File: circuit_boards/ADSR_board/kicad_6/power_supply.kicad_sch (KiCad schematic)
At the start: 21 parts, among them J5 power_entry, U101 TL072, U201 TL072, U301 TL072, U401 TL072

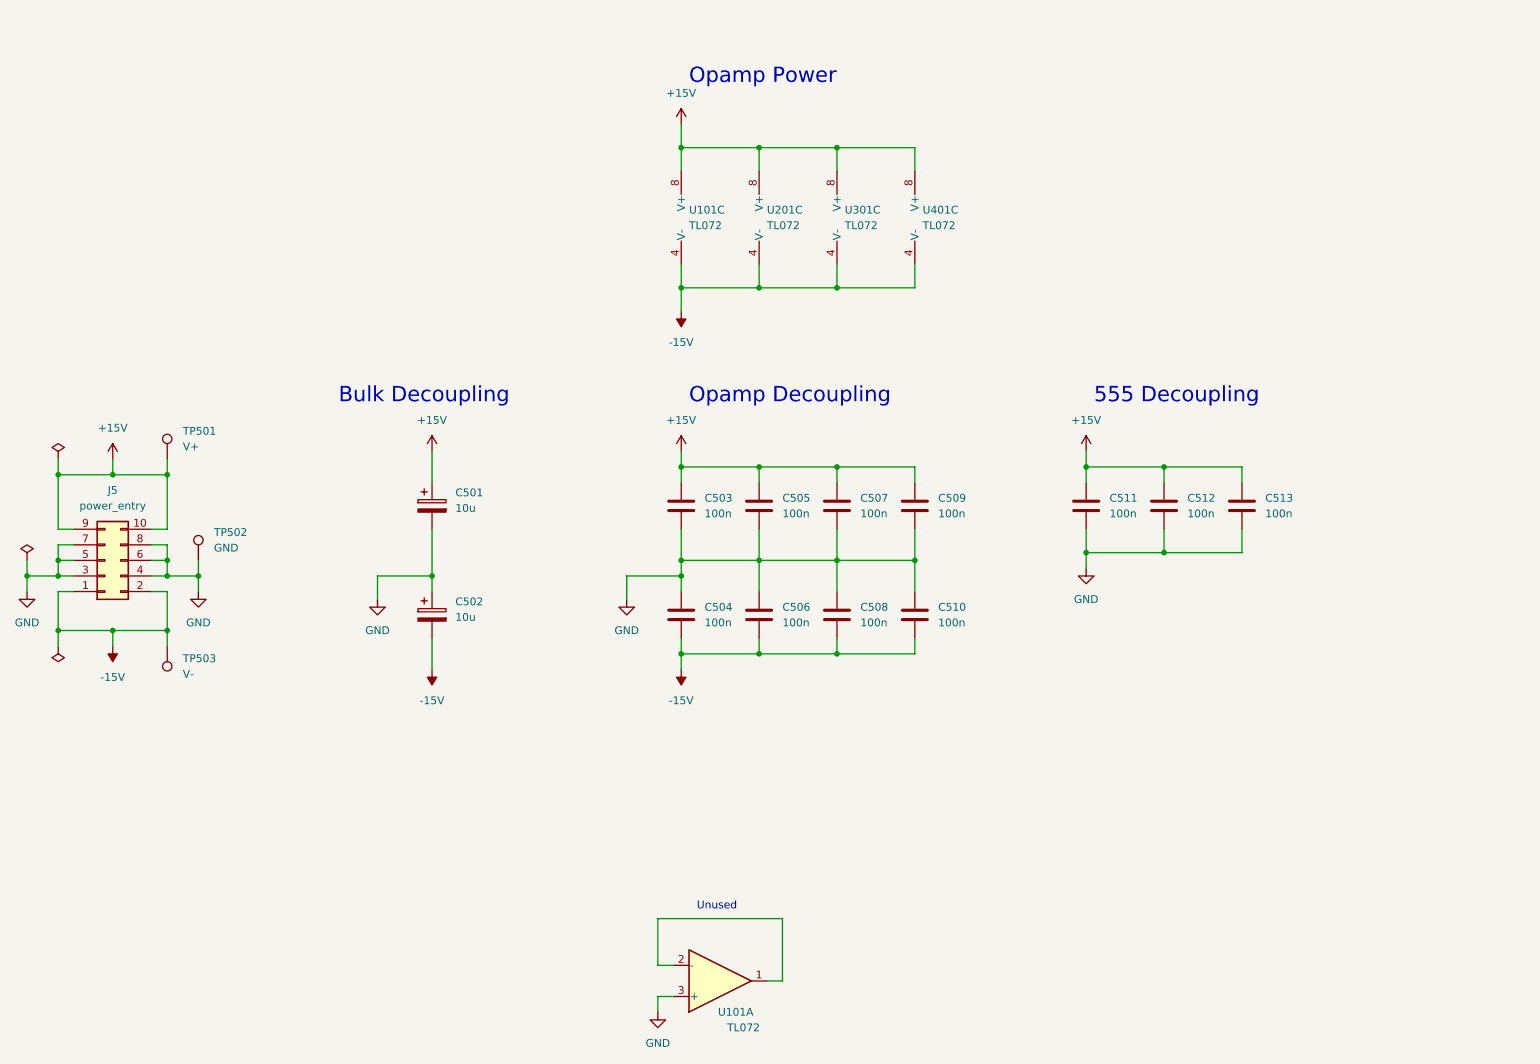
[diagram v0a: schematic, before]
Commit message: Upgrade ADSR to analog swiitch version
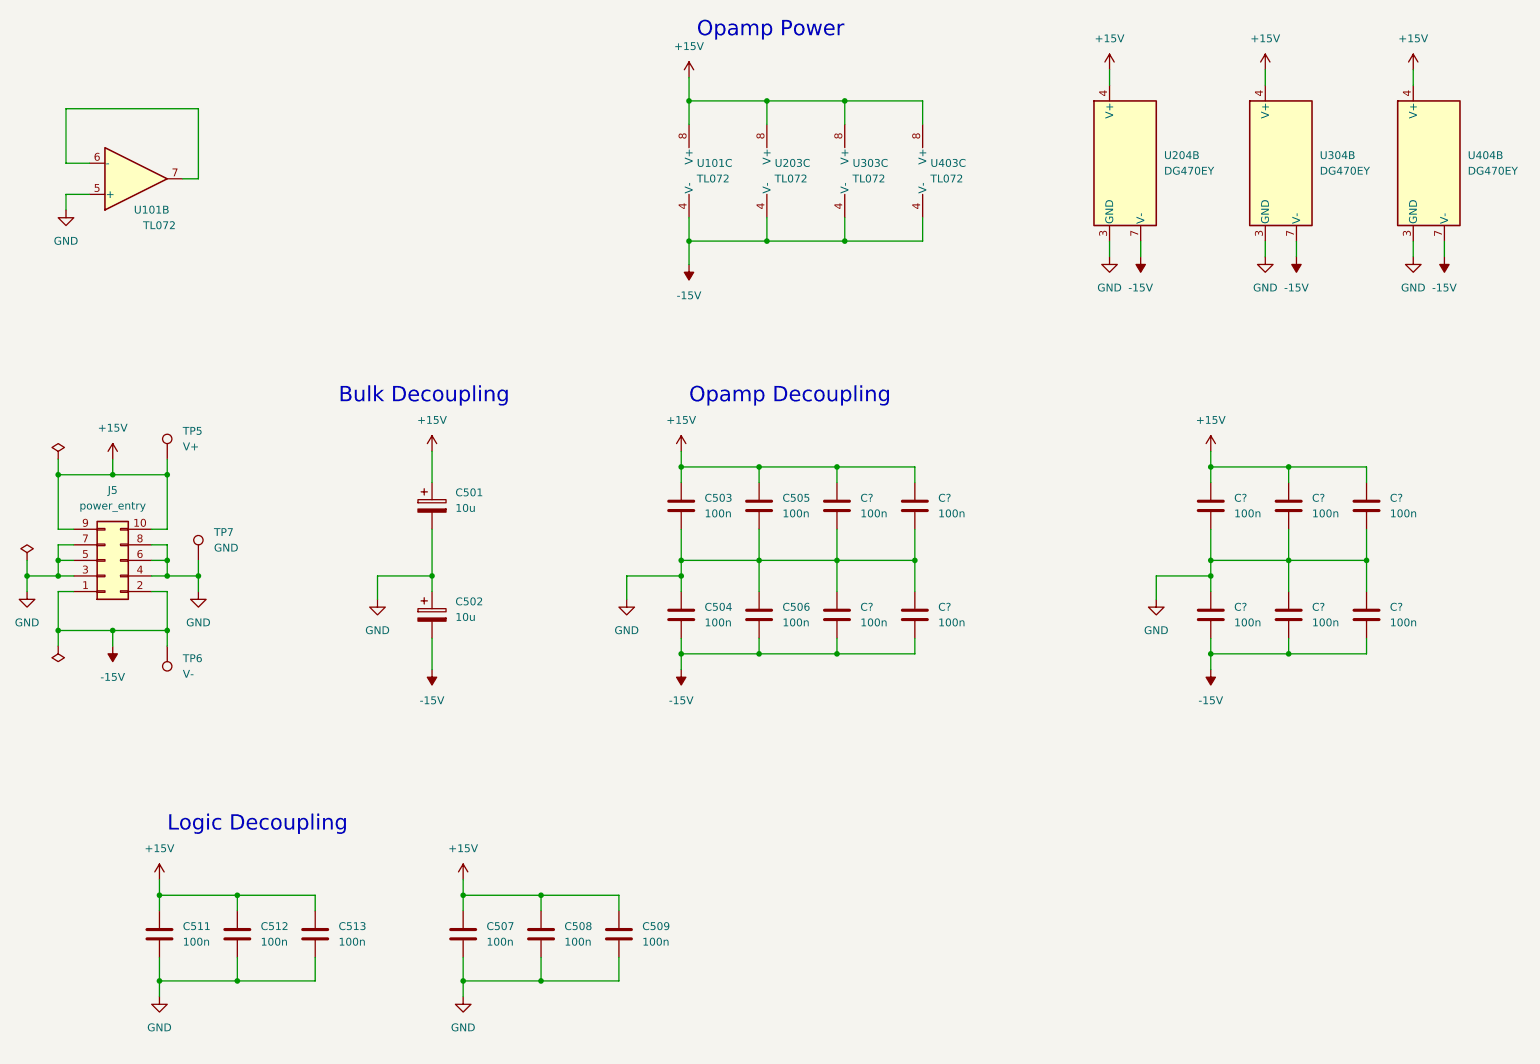
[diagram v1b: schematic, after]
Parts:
- removed C510: 100n, Capacitor_SMD:C_0805_2012Metric, symbol Device:C
- removed unit 1 of U101
- removed U301, U401: TL072, Package_SO:SO-8_5.3x6.2mm_P1.27mm, symbol Amplifier_Operational:TL072
- added C? (x10): 100n, Capacitor_SMD:C_0805_2012Metric, symbol Device:C
- added unit 2 of U101
- added U204, U304, U404: DG470EY, Package_SO:SOIC-8_3.9x4.9mm_P1.27mm, symbol custom_symbols:DG470EY
- added U303, U403: TL072, Package_SO:SOIC-8_3.9x4.9mm_P1.27mm, symbol Amplifier_Operational:TL072
- U101: footprint Package_SO:SO-8_5.3x6.2mm_P1.27mm -> Package_SO:SOIC-8_3.9x4.9mm_P1.27mm
- U203: renamed from U201; footprint Package_SO:SO-8_5.3x6.2mm_P1.27mm -> Package_SO:SOIC-8_3.9x4.9mm_P1.27mm
- renumbered TP501 to TP5, TP503 to TP6, TP502 to TP7
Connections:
- net +15V: now also C508.1, C?.1, C?.1, C?.1, C?.1, C?.1, U204.4 (V+), U303.8 (V+), U304.4 (V+), U403.8 (V+), U404.4 (V+)
- net -15V: now also C?.2, C?.2, C?.2, C?.2, C?.2, U204.7 (V-), U303.4 (V-), U304.7 (V-), U403.4 (V-), U404.7 (V-); no longer C508.2
- net GND: now also C508.2, C?.1, C?.1, C?.1, C?.1, C?.1, C?.2, C?.2, C?.2, C?.2, C?.2, U101.5 (+), U204.3 (GND), U304.3 (GND), U404.3 (GND); no longer C508.1
- new net: U101.6 (-), U101.7
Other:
- note added: "Logic Decoupling"
- note removed: "555 Decoupling"
- note removed: "Unused"
- moved on the sheet: C511, C512, C513, U101C, U203C
